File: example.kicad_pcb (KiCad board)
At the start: 2 copper layers, 40 x 25 mm, 39 parts, among them J1 USB_C_Receptacle_USB2.0_16P, J2 SSD1309 24-Pin Connector, J3 SSD1327 16-Pin Connector, J4 SSD1322 30-Pin Connector, U1 AP2112K-3.3, U2 ESP32-S3-WROOM-1, U3 MT3608

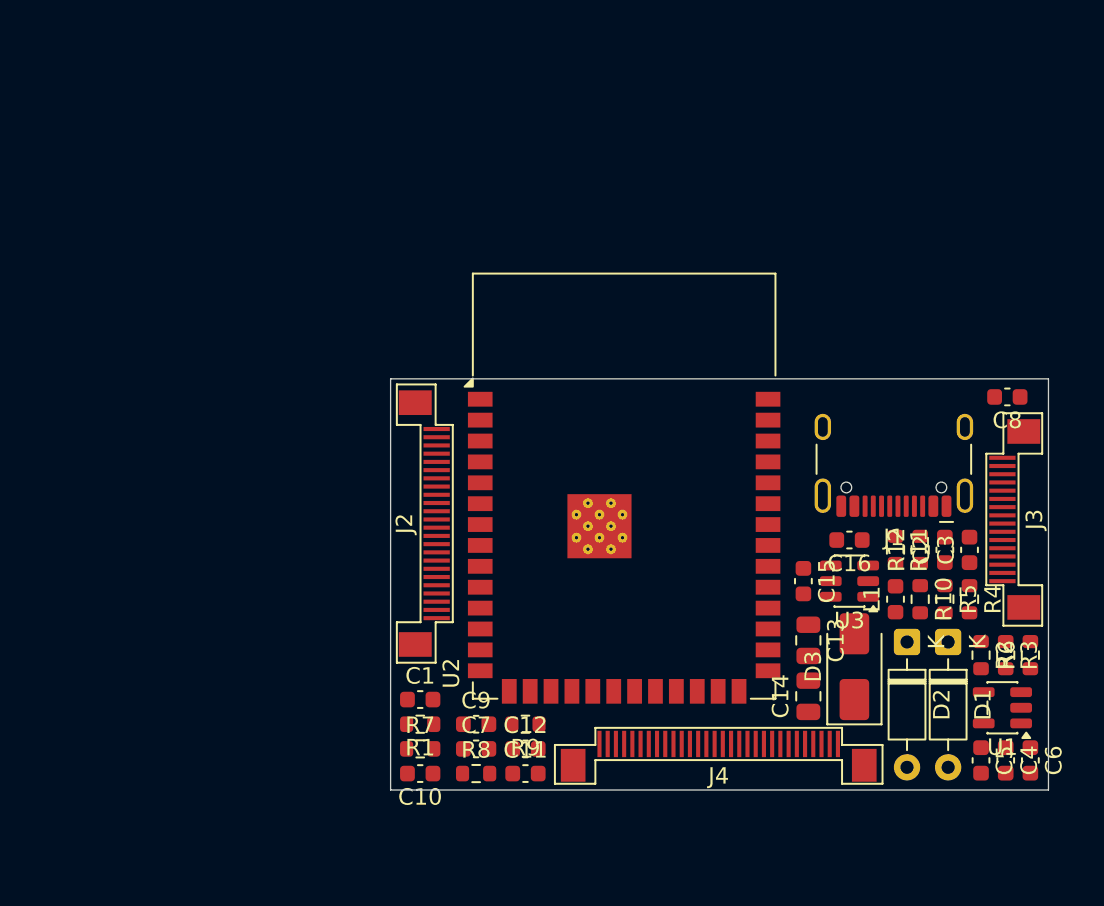
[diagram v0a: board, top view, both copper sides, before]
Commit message: PCB layout part 2
Really dense layout but incomplete; can't connect GND nodes
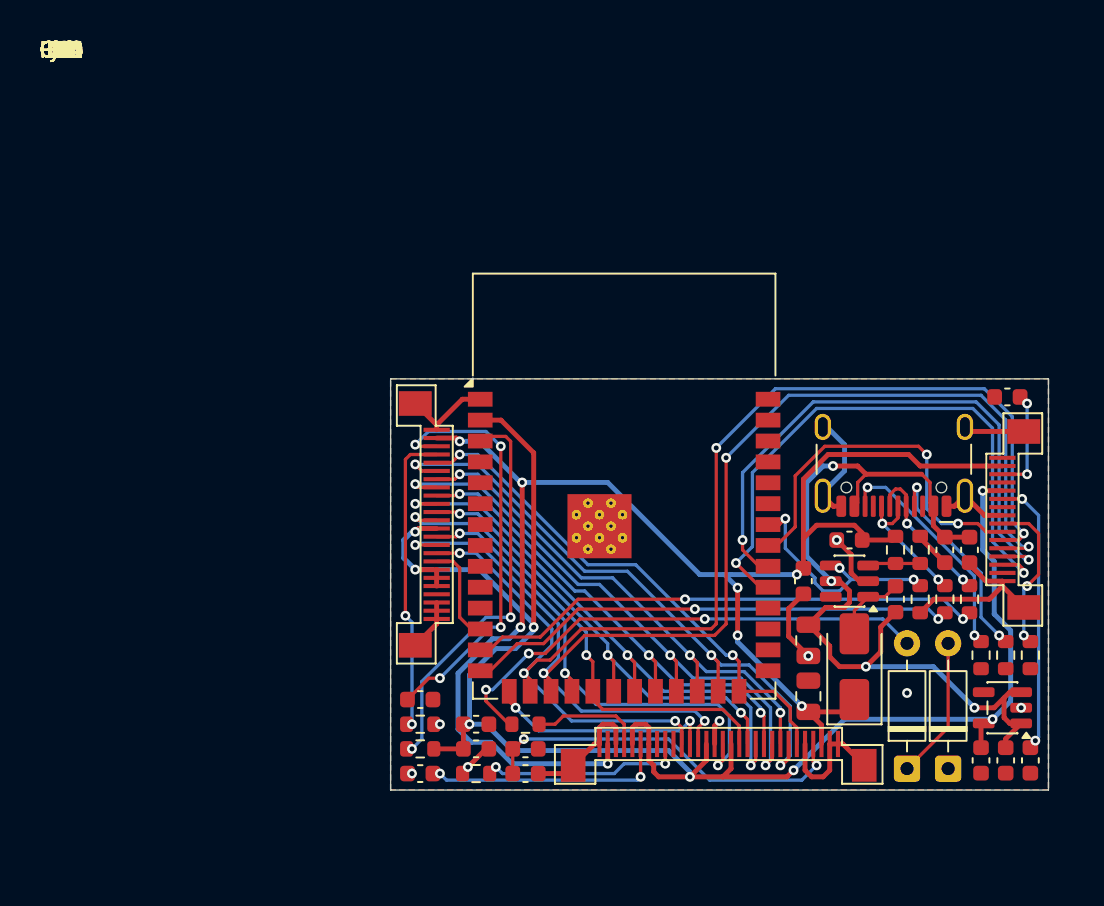
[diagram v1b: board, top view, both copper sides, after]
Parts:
- moved D1 8.10 mm to (51.4, 43.7), turned to 90 degrees
- moved D2 8.10 mm to (53.9, 43.7), turned to 90 degrees
- moved J2 0.05 mm to (22.8, 28.9)
- turned C2 to -90 degrees
- turned C3 to -90 degrees
- turned R7 to 180 degrees
- turned R9 to 0 degrees
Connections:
- U2 pad 34: unconnected-(U2-IO41-Pad34) -> /MT3608/EN
- U2 pad 9: /MT3608/EN -> unconnected-(U2-IO16-Pad9)
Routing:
- net +3V3: track 0.00 -> 107.1 mm, vias 0 -> 8
- net +12V: track 0.00 -> 95.2 mm, vias 0 -> 8
- net /DC: track 0.00 -> 81.3 mm, vias 0 -> 5
- net /RES: track 0.00 -> 78.3 mm, vias 0 -> 5
- net GND: track 0.00 -> 62.6 mm, vias 0 -> 8
- net +5V: track 0.00 -> 51.6 mm, vias 0 -> 4
- net /D6: track 0.00 -> 38.1 mm, vias 0 -> 3
- net /MOSI: track 0.00 -> 36.5 mm, vias 0 -> 2
- net /D4: track 0.00 -> 36.1 mm, vias 0 -> 3
- net /CLK: track 0.00 -> 35.4 mm, vias 0 -> 2
- net /D2: track 0.00 -> 34.2 mm, vias 0 -> 3
- net Net-(U2-USB_D-): track 0.00 -> 31.7 mm, vias 0 -> 2
- net /D7: track 0.00 -> 31.5 mm, vias 0 -> 2
- net /D5: track 0.00 -> 31.5 mm, vias 0 -> 3
- net Net-(D1-A): track 0.00 -> 30.8 mm, vias 0 -> 3
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- added copper zone on B.Cu, net GND
- added copper zone on F.Cu, net GND

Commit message: PCB layout part 3
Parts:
- moved C7 34.0 mm to (52.9, 22.8)
- moved C9 34.0 mm to (52.9, 21.3)
- moved D2 32.7 mm to (21.5, 48.3), turned to 0 degrees
- moved R10 30.8 mm to (21.9, 39.1)
- moved D1 30.0 mm to (21.5, 45.8), turned to 0 degrees
- moved R12 28.0 mm to (24.8, 36.1)
- moved R11 25.1 mm to (26.3, 36.1)
- moved C13 24.2 mm to (22.1, 42.3)
- moved U3 23.8 mm to (25.2, 39.3)
- moved C16 22.4 mm to (25.5, 30.3)
- moved D3 22.1 mm to (26.7, 42.8), turned to 0 degrees
- moved L1 21.6 mm to (31.7, 43.7), turned to 180 degrees
- moved R7 21.0 mm to (26.3, 22.0), turned to -90 degrees
- moved C14 20.5 mm to (25.7, 33.6), turned to 180 degrees
- moved C6 19.9 mm to (55.2, 23.6), turned to 90 degrees
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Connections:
- U2 pad 11: unconnected-(U2-IO18-Pad11) -> /MT3608/EN
- U2 pad 15: /CS_1322 -> /RES
- U2 pad 16: /RES -> /CS_1322
- U2 pad 34: /MT3608/EN -> unconnected-(U2-IO41-Pad34)
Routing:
- net Net-(D1-A): track 30.8 -> 2.00 mm, vias 3 -> 0
- net /MOSI: track 36.5 -> 8.98 mm, vias 2 -> 0
- net /CLK: track 35.4 -> 8.57 mm, vias 2 -> 0
- net /DC: track 81.3 -> 55.2 mm, vias 5 -> 3
- net GND: track 62.6 -> 39.2 mm, vias 8 -> 15
- net Net-(J2-VCOMH): track 25.7 -> 2.68 mm, vias 4 -> 0
- net /RES: track 78.3 -> 55.9 mm, vias 5 -> 3
- net Net-(J4-VCOMH): track 23.0 -> 3.72 mm, vias 2 -> 0
- net Net-(U2-EN): track 24.5 -> 5.35 mm, vias 2 -> 0
- net Net-(U2-USB_D+): track 30.5 -> 48.3 mm
- net Net-(J2-IREF): track 18.6 -> 2.00 mm, vias 2 -> 0
- net Net-(U2-USB_D-): track 31.7 -> 48.0 mm
- net /CS_1327: track 22.7 -> 9.17 mm, vias 2 -> 0
- net Net-(J4-VDD): track 14.4 -> 2.01 mm, vias 2 -> 0
- net Net-(J3-VDD): track 16.9 -> 5.05 mm, vias 2 -> 0
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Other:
- board size 40 x 25 mm -> 40 x 30 mm

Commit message: PCB layout part 4
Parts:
- D1, D2: footprint Diode_THT:D_DO-35_SOD27_P7.62mm_Horizontal -> Diode_SMD:D_SOD-123
- moved D3 3.80 mm to (28.4, 46.2), turned to 90 degrees
- moved D2 3.22 mm to (24.3, 46.7)
- moved D1 3.13 mm to (24.3, 44.4)
- moved C13 2.80 mm to (24.9, 42.2), turned to 180 degrees
- moved R10 0.64 mm to (22.4, 39.5)
- moved U3 0.20 mm to (25.2, 39.5)
- moved C15 0.20 mm to (25.5, 32.0)
- moved C16 0.20 mm to (25.5, 30.5)
- moved C14 0.20 mm to (25.7, 33.8)
- moved R11 0.20 mm to (26.3, 36.3)
- moved R12 0.20 mm to (24.8, 36.3)
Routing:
- net Net-(D1-K): track 8.66 -> 4.25 mm
- net GND: track 39.2 -> 34.9 mm
- net Net-(D1-A): track 2.00 -> 5.84 mm
- net +5V: track 58.4 -> 60.9 mm, vias 3 -> 2
- net +12V: track 88.8 -> 90.1 mm, vias 7 -> 6
- net /RW: track 32.6 -> 31.2 mm
- net Net-(D3-A): track 6.11 -> 7.32 mm
- net /CS_1309: track 15.5 -> 16.6 mm
- net +3V3: track 106.9 -> 105.9 mm
- net /MT3608/EN: track 12.7 -> 12.0 mm, vias 2 -> 0
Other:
- board text added: "Jonathan Ho 2026-10-02"
- board text added: "OLED Screen Tester"
